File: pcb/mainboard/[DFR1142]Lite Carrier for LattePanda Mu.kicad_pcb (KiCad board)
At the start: 4 copper layers, 0 parts

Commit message: before i start jul 10th
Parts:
- added A1: LattePanda_Mu, Module_LattePanda:LattePanda_Module_H8.0mm_Horizontal, F.Cu at (148.0, 86.5)
- added BT1: Battery_Cell, A_HDJ_Library:Battery_Holder_CR1220_S8411-45R, F.Cu at (84.0, 114.3)
- added C17: 100nF/50V, A_HDJ_Library:C_0402_1005Metric, F.Cu at (172.5, 94.0)
- added C18: 100nF/50V, A_HDJ_Library:C_0402_1005Metric, F.Cu at (171.5, 94.0)
- added C19: 100nF/50V, A_HDJ_Library:C_0402_1005Metric, F.Cu at (170.5, 94.0)
- added C20: 100nF/50V, A_HDJ_Library:C_0402_1005Metric, F.Cu at (169.5, 94.0)
- added C21: 100nF/50V, A_HDJ_Library:C_0402_1005Metric, F.Cu at (168.5, 94.0)
- added C22: 100nF/50V, A_HDJ_Library:C_0402_1005Metric, F.Cu at (167.5, 94.0)
- added C23: 100nF/50V, A_HDJ_Library:C_0402_1005Metric, F.Cu at (166.5, 94.0)
- added C24: 100nF/50V, A_HDJ_Library:C_0402_1005Metric, F.Cu at (165.5, 94.0)
- added C25: 100nF/50V, A_HDJ_Library:C_0402_1005Metric, F.Cu at (17.4, 95.5)
- added C26: 100nF/50V, A_HDJ_Library:C_0402_1005Metric, F.Cu at (117.5, 93.5)
- added C27: 100nF/50V, A_HDJ_Library:C_0402_1005Metric, F.Cu at (116.5, 93.5)
- added C28: 100nF/50V, A_HDJ_Library:C_0402_1005Metric, F.Cu at (120.0, 93.5)
- added C29: 100nF/50V, A_HDJ_Library:C_0402_1005Metric, F.Cu at (119.0, 93.5)
- added C30: 22uF/10V, A_HDJ_Library:C_0603_1608Metric, F.Cu at (185.0, 113.0)
- added C31: 22uF/10V, A_HDJ_Library:C_0603_1608Metric, F.Cu at (179.0, 146.0)
- added C32: 22uF/10V, A_HDJ_Library:C_0603_1608Metric, F.Cu at (179.0, 130.0)
- added C49: 220nF/50V, A_HDJ_Library:C_0402_1005Metric, F.Cu at (141.0, 131.5)
- added C50: 220nF/50V, A_HDJ_Library:C_0402_1005Metric, F.Cu at (142.0, 131.5)
- added C51: 10uF/10V, A_HDJ_Library:C_0402_1005Metric, F.Cu at (132.5, 131.0)
- added C52: 100nF/50V, A_HDJ_Library:C_0402_1005Metric, F.Cu at (132.5, 132.0)
- added C53: 10uF/10V, A_HDJ_Library:C_0402_1005Metric, F.Cu at (132.5, 129.0)
- added C54: 100nF/50V, A_HDJ_Library:C_0402_1005Metric, F.Cu at (132.5, 130.0)
- added C55: 220nF/50V, A_HDJ_Library:C_0402_1005Metric, F.Cu at (120.4, 116.8)
- added C56: 220nF/50V, A_HDJ_Library:C_0402_1005Metric, F.Cu at (120.4, 117.8)
- added C57: 10uF/10V, A_HDJ_Library:C_0402_1005Metric, F.Cu at (113.4, 133.8)
- added C58: 100nF/50V, A_HDJ_Library:C_0402_1005Metric, F.Cu at (113.4, 132.8)
- added C59: 10uF/10V, A_HDJ_Library:C_0402_1005Metric, F.Cu at (113.4, 131.8)
- added C60: 100nF/50V, A_HDJ_Library:C_0402_1005Metric, F.Cu at (113.4, 130.8)
- added C64: 22uF/10V, A_HDJ_Library:C_0603_1608Metric, F.Cu at (22.5, 113.8)
- added C65: 22uF/10V, A_HDJ_Library:C_0603_1608Metric, F.Cu at (28.0, 138.5)
- added C66: 1uF/16V, A_HDJ_Library:C_0402_1005Metric, F.Cu at (14.5, 25.5)
- added C67: 22uF/10V, A_HDJ_Library:C_0603_1608Metric, F.Cu at (24.0, 113.8)
- added C68: 22uF/10V, A_HDJ_Library:C_0603_1608Metric, F.Cu at (28.0, 137.0)
- added C70: 100nF/50V, A_HDJ_Library:C_0402_1005Metric, F.Cu at (18.5, 110.0)
- added C71: 100nF/50V, A_HDJ_Library:C_0402_1005Metric, F.Cu at (23.5, 136.0)
- added C72: 12pF/50V, Capacitor_SMD:C_0402_1005Metric, F.Cu at (-38.2, 97.7)
- added C73: 12pF/50V, Capacitor_SMD:C_0402_1005Metric, F.Cu at (-38.2, 99.7)
- added C74: 22uF/10V, A_HDJ_Library:C_0603_1608Metric, F.Cu at (25.7, 107.0)
- added C75: 22uF/10V, A_HDJ_Library:C_0603_1608Metric, F.Cu at (31.8, 136.0)
- added C76: 22uF/10V, A_HDJ_Library:C_0603_1608Metric, F.Cu at (25.7, 108.5)
- added C77: 22uF/10V, A_HDJ_Library:C_0603_1608Metric, F.Cu at (31.8, 134.5)
- added C78: 100nF/50V, A_HDJ_Library:C_0402_1005Metric, F.Cu at (25.7, 102.5)
- added C79: 100nF/50V, A_HDJ_Library:C_0402_1005Metric, F.Cu at (31.8, 137.5)
- added C80: 22uF/10V, A_HDJ_Library:C_0603_1608Metric, F.Cu at (25.7, 104.0)
- added C81: 22uF/10V, A_HDJ_Library:C_0603_1608Metric, F.Cu at (31.8, 131.5)
- added C82: 22uF/10V, A_HDJ_Library:C_0603_1608Metric, F.Cu at (25.7, 105.5)
- added C83: 22uF/10V, A_HDJ_Library:C_0603_1608Metric, F.Cu at (31.8, 133.0)
- added C86: 22uF/10V, A_HDJ_Library:C_0603_1608Metric, F.Cu at (194.2, 80.5)
- added D1: ESD5V0B03, A_HDJ_Library:D_0402_1005Metric, F.Cu at (186.0, 98.5)
- added D15: SS54, A_HDJ_Library:D_SMA, F.Cu at (25.5, 120.5)
- added D16: SS54, A_HDJ_Library:D_SMA, F.Cu at (29.0, 120.5)
- added D17: SS54, A_HDJ_Library:D_SMA, F.Cu at (32.5, 120.5)
- added D2: ESD5V0B03, A_HDJ_Library:D_0402_1005Metric, F.Cu at (186.5, 102.5)
- added D21: ESD5V0B03, A_HDJ_Library:D_0402_1005Metric, F.Cu at (19.5, 25.5)
- added D22: LED_G, A_HDJ_Library:LED_0603_1608Metric, F.Cu at (-8.50, 85.5)
- added D24: 3V3 Izt=5mA, A_HDJ_Library:D_SOD-323, F.Cu at (-25.8, 103.9)
- added D3: ESD5V0B03, A_HDJ_Library:D_0402_1005Metric, F.Cu at (186.0, 99.5)
- added D4: 1N5819WS, A_HDJ_Library:D_SOD-323, F.Cu at (21.4, 75.0)
- added D5: ESD5V0B03, A_HDJ_Library:D_0402_1005Metric, F.Cu at (131.5, 93.5)
- added D6: ESD5V0B03, A_HDJ_Library:D_0402_1005Metric, F.Cu at (130.5, 93.5)
- added D7: ESD5V0B03, A_HDJ_Library:D_0402_1005Metric, F.Cu at (133.5, 93.5)
- added D8: ESD5V0B03, A_HDJ_Library:D_0402_1005Metric, F.Cu at (132.5, 93.5)
- added D9: LED_G, A_HDJ_Library:LED_0603_1608Metric, F.Cu at (131.0, 146.0)
- added F1: 6V/50mA, A_HDJ_Library:R_0603_1608Metric, F.Cu at (2.89, 95.9)
- added F2: 6V/1A, A_HDJ_Library:Fuse_0805_2012Metric, F.Cu at (188.5, 113.0)
- added F4: 6V/2A, A_HDJ_Library:R_0805_2012Metric, F.Cu at (183.1, 146.0)
- added F5: 6V/2A, A_HDJ_Library:Fuse_0805_2012Metric, F.Cu at (181.0, 127.0)
- added F78: 6V/1A, A_HDJ_Library:Fuse_0805_2012Metric, F.Cu at (197.0, 79.5)
- added FID1: Fiducial, A_HDJ_Library:Fiducial_0.5mm_Mask1mm, F.Cu at (50.0, 54.5)
- added FID2: Fiducial, A_HDJ_Library:Fiducial_0.5mm_Mask1mm, F.Cu at (50.0, 57.0)
- added H1: MountingHole_Pad, A_HDJ_Library:MountingHole_3.2mm_M3_Pad_Via, F.Cu at (171.0, 144.0)
- added H2: MountingHole_Pad, A_HDJ_Library:MountingHole_3.2mm_M3_Pad_Via, F.Cu at (194.5, 59.0)
- added H3: MountingHole_Pad, A_HDJ_Library:MountingHole_3.2mm_M3_Pad_Via, F.Cu at (109.5, 59.0)
- added H4: MountingHole_Pad, A_HDJ_Library:MountingHole_3.2mm_M3_Pad_Via, F.Cu at (110.0, 144.0)
- added H5: MountingHole_Pad, A_HDJ_Library:MountingHole_3mm_M2_Pad_TopOnly, F.Cu at (-20.1, 56.3)
- added H6: MountingHole_Pad, A_HDJ_Library:MountingHole_3mm_M2_Pad_TopOnly, F.Cu at (-20.1, 63.5)
- added J1: Conn_01x03_Pin, A_HDJ_Library:PinHeader_1x03_P2.54mm_Vertical, F.Cu at (118.0, 61.0)
- added J10: Conn_01x03_Pin, A_HDJ_Library:PinHeader_1x03_P2.54mm_Vertical, F.Cu at (143.5, 63.0)
- added J11: Conn_01x03_Pin, A_HDJ_Library:PinHeader_1x03_P2.54mm_Vertical, F.Cu at (139.8, 63.0)
- added J12: Conn_01x04_Pin, A_HDJ_Library:PinHeader_1x04_P2.54mm_Vertical, F.Cu at (154.2, 60.6)
- added J13: Conn_01x04_Pin, A_HDJ_Library:PinHeader_1x04_P2.54mm_Vertical, F.Cu at (154.2, 57.0)
- added J14: Conn_01x03_Pin, A_HDJ_Library:PinHeader_1x03_P2.54mm_Vertical, F.Cu at (136.1, 63.0)
- added J15: Bus_M.2_Socket_M, A_HDJ_Library:PCIe_M.2_Connectors_P=0.5mm_H=4.2mm_KeyM, F.Cu at (139.0, 139.0)
- added J16: Bus_M.2_Socket_E, A_HDJ_Library:PCIe_M.2_Connectors_P=0.5mm_H=4.2mm_KeyE, F.Cu at (116.9, 108.8)
- added J3: HDMI_A, A_HDJ_Library:HDMI_A_Molex_208658-1001_Horizontal, F.Cu at (192.6, 94.8)
- added J7: Conn_01x04_Pin, A_HDJ_Library:PinHeader_1x04_P2.54mm_Vertical, F.Cu at (167.7, 60.6)
- added J78: Conn_01x02_Pin, Connector_PinHeader_2.54mm:PinHeader_1x02_P2.54mm_Vertical, F.Cu at (-33.8, 101.6)
- added J79: USB3_A, Connector_USB:USB3_A_Molex_48393-001, F.Cu at (189.3, 143.0)
- added J8: Conn_01x03_Pin, A_HDJ_Library:PinHeader_1x03_P2.54mm_Vertical, F.Cu at (147.1, 63.0)
- added J80: USB3_A, Connector_USB:USB3_A_Molex_48393-001, F.Cu at (189.3, 127.0)
- added J81: USB_C_Receptacle_USB2.0_16P, Connector_USB:USB_C_Receptacle_GCT_USB4085, F.Cu at (192.6, 112.7)
- added J82: Conn_01x04_Pin, Connector_PinHeader_2.54mm:PinHeader_1x04_P2.54mm_Vertical, F.Cu at (193.5, 77.1)
- added J83: Conn_01x02_Pin, Connector_PinHeader_2.54mm:PinHeader_1x02_P2.54mm_Vertical, F.Cu at (17.0, 26.5)
- added J9: Conn_01x04_Pin, A_HDJ_Library:PinHeader_1x04_P2.54mm_Vertical, F.Cu at (167.7, 57.0)
- added JP1: Jumper_3_Bridged12, A_HDJ_Library:PinHeader_1x03_P2.54mm_Vertical, F.Cu at (13.0, 139.0)
- added L1: 2.2uH/4.3A, A_HDJ_Library:L_Sunlord_SWPA4020S, F.Cu at (21.0, 106.5)
- added L2: 2.2uH/4.3A, A_HDJ_Library:L_Sunlord_SWPA4020S, F.Cu at (26.5, 133.0)
- added Q1: 2N7002, A_HDJ_Library:SOT-23, F.Cu at (181.5, 102.0)
- added Q2: 2SK3018, A_HDJ_Library:SOT-23, F.Cu at (7.81, 83.3)
- added Q3: 2SK3018, A_HDJ_Library:SOT-23, F.Cu at (185.1, 106.0)
- added Q4: 2SK3018, A_HDJ_Library:SOT-23, F.Cu at (168.5, 105.4)
- added Q8: 2N7002, A_HDJ_Library:SOT-23, F.Cu at (-11.5, 84.5)
- added R1: 1K/1%, A_HDJ_Library:R_0402_1005Metric, F.Cu at (-15.0, 53.7)
- added R10: 470R/1%, A_HDJ_Library:R_0402_1005Metric, F.Cu at (168.5, 101.5)
- added R11: 1K/1%, A_HDJ_Library:R_0402_1005Metric, F.Cu at (186.0, 101.0)
- added R13: 470R/1%, A_HDJ_Library:R_0402_1005Metric, F.Cu at (169.5, 101.5)
- added R14: 470R/1%, A_HDJ_Library:R_0402_1005Metric, F.Cu at (170.5, 101.5)
- added R15: 2.2K/1%, A_HDJ_Library:R_0402_1005Metric, F.Cu at (18.5, 77.0)
- added R16: 470R/1%, A_HDJ_Library:R_0402_1005Metric, F.Cu at (171.5, 101.5)
- added R17: 470R/1%, A_HDJ_Library:R_0402_1005Metric, F.Cu at (172.5, 101.5)
- added R18: 2.2K/1%, A_HDJ_Library:R_0402_1005Metric, F.Cu at (17.5, 77.0)
- added R19: 2.2K/1%, A_HDJ_Library:R_0402_1005Metric, F.Cu at (167.0, 108.0)
- added R2: 10K/1%, A_HDJ_Library:R_0402_1005Metric, F.Cu at (147.5, 93.5)
- added R27: 0R/1%, A_HDJ_Library:R_0402_1005Metric, F.Cu at (143.5, 146.0)
- added R29: 0R/1%, A_HDJ_Library:R_0402_1005Metric, F.Cu at (147.5, 146.0)
- added R3: 2.2K/1%, A_HDJ_Library:R_0402_1005Metric, F.Cu at (11.7, 83.6)
- added R30: 2.2K/1%, A_HDJ_Library:R_0402_1005Metric, F.Cu at (134.5, 146.0)
- added R32: 0R/1%, A_HDJ_Library:R_0402_1005Metric, F.Cu at (120.0, 121.5)
- added R33: 0R/1%, A_HDJ_Library:R_0402_1005Metric, F.Cu at (106.5, 121.5)
- added R34: 10K/1%, A_HDJ_Library:R_0402_1005Metric, F.Cu at (109.4, 131.8)
- added R35: 10K/1%, A_HDJ_Library:R_0402_1005Metric, F.Cu at (109.4, 133.1)
- added R4: 1M/1%, A_HDJ_Library:R_0402_1005Metric, F.Cu at (179.0, 102.0)
- added R46: 100R/1%, A_HDJ_Library:R_0402_1005Metric, F.Cu at (29.0, 140.0)
- added R47: 1K/1%, A_HDJ_Library:R_0402_1005Metric, F.Cu at (-20.9, 98.7)
- added R48: 100R/1%, A_HDJ_Library:R_0402_1005Metric, F.Cu at (20.0, 23.5)
- added R49: 10K/1%, A_HDJ_Library:R_0402_1005Metric, F.Cu at (-14.5, 84.5)
- added R5: 2.2K/1%, A_HDJ_Library:R_0402_1005Metric, F.Cu at (11.7, 87.6)
- added R50: 10K/1%, Resistor_SMD:R_0402_1005Metric, F.Cu at (20.0, 22.0)
- added R51: 100K/1%, A_HDJ_Library:R_0402_1005Metric, F.Cu at (26.5, 140.5)
- added R52: 2.2K/1%, A_HDJ_Library:R_0402_1005Metric, F.Cu at (-8.00, 87.5)
- added R53: 2.2K/1%, A_HDJ_Library:R_0402_1005Metric, F.Cu at (-18.0, 100.7)
- added R57: 75K/1%, A_HDJ_Library:R_0402_1005Metric, F.Cu at (17.5, 115.5)
- added R58: 10K/1%, A_HDJ_Library:R_0402_1005Metric, F.Cu at (17.5, 116.5)
- added R59: 21.5K/1%, A_HDJ_Library:R_0402_1005Metric, F.Cu at (23.5, 141.5)
- added R6: 21.5K/1%, A_HDJ_Library:R_0402_1005Metric, F.Cu at (184.5, 102.0)
- added R60: 4.7K/1%, A_HDJ_Library:R_0402_1005Metric, F.Cu at (20.5, 139.0)
- added R7: 470R/1%, A_HDJ_Library:R_0402_1005Metric, F.Cu at (165.5, 101.5)
- added R76: 100K/1%, A_HDJ_Library:R_0402_1005Metric, F.Cu at (-15.0, 57.7)
- added R77: 100K/1%, A_HDJ_Library:R_0402_1005Metric, F.Cu at (-15.0, 59.7)
- added R78: 10K/1%, Resistor_SMD:R_0402_1005Metric, F.Cu at (-15.0, 61.7)
- added R79: 10K/1%, Resistor_SMD:R_0402_1005Metric, F.Cu at (-15.0, 63.7)
- added R8: 470R/1%, A_HDJ_Library:R_0402_1005Metric, F.Cu at (166.5, 101.5)
- added R80: 5.1K/1%, A_HDJ_Library:R_0402_1005Metric, F.Cu at (189.5, 110.5)
- added R81: 5.1K/1%, A_HDJ_Library:R_0402_1005Metric, F.Cu at (189.5, 109.5)
- added R9: 470R/1%, A_HDJ_Library:R_0402_1005Metric, F.Cu at (167.5, 101.5)
- added TP13: TestPoint, A_HDJ_Library:TestPoint_Pad_D1.5mm, F.Cu at (-37.9, 89.0)
- added TP2: TestPoint, A_HDJ_Library:TestPoint_Pad_D1.5mm, F.Cu at (123.0, 143.0)
- added TP4: TestPoint, A_HDJ_Library:TestPoint_Pad_D1.5mm, F.Cu at (-37.9, 78.4)
- added TP5: TestPoint, A_HDJ_Library:TestPoint_Pad_D1.5mm, F.Cu at (-37.9, 82.0)
- added TP6: TestPoint, A_HDJ_Library:TestPoint_Pad_D1.5mm, F.Cu at (-37.9, 85.5)
- added TP7: TestPoint, A_HDJ_Library:TestPoint_Pad_D1.5mm, F.Cu at (150.5, 94.5)
- added U1: TPAZ1023-04F, A_HDJ_Library:Diodes_UDFN-10_1.0x2.5mm_P0.5mm, F.Cu at (193.5, 84.9)
- added U10: ULC0524P, A_HDJ_Library:Diodes_UDFN-10_1.0x2.5mm_P0.5mm, F.Cu at (144.6, 55.2)
- added U11: ULC0524P, A_HDJ_Library:Diodes_UDFN-10_1.0x2.5mm_P0.5mm, F.Cu at (178.1, 56.5)
- added U12: ULC0524P, A_HDJ_Library:Diodes_UDFN-10_1.0x2.5mm_P0.5mm, F.Cu at (141.1, 55.2)
- added U15: SY8253ADC, A_HDJ_Library:TSOT-23-6, F.Cu at (18.4, 112.5)
- added U16: SY8253ADC, A_HDJ_Library:TSOT-23-6, F.Cu at (23.5, 138.5)
- added U2: TPAZ1023-04F, A_HDJ_Library:Diodes_UDFN-10_1.0x2.5mm_P0.5mm, F.Cu at (197.5, 84.9)
- added U3: ULC0524P, A_HDJ_Library:Diodes_UDFN-10_1.0x2.5mm_P0.5mm, F.Cu at (182.6, 133.0)
- added U4: ULC0524P, A_HDJ_Library:Diodes_UDFN-10_1.0x2.5mm_P0.5mm, F.Cu at (197.5, 73.3)
- added U5: ULC0524P, A_HDJ_Library:Diodes_UDFN-10_1.0x2.5mm_P0.5mm, F.Cu at (183.1, 122.0)
- added U9: ULC0524P, A_HDJ_Library:Diodes_UDFN-10_1.0x2.5mm_P0.5mm, F.Cu at (178.1, 61.5)
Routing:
- net /Gigabit Ethernet/MDI3+: track 2.23 -> 0.00 mm
- net /Gigabit Ethernet/MDI1-: track 1.67 -> 0.00 mm
- net /Gigabit Ethernet/MDI1+: track 1.58 -> 0.00 mm
- net /Gigabit Ethernet/MDI2-: track 1.30 -> 0.00 mm
- net /Gigabit Ethernet/MDI2+: track 1.21 -> 0.00 mm
- net /Gigabit Ethernet/MDI0+: track 0.97 -> 0.00 mm
- net /LattePanda Module/HSIO_9_TX+: track 0.97 -> 0.00 mm
- net /LattePanda Module/HSIO_11_TX+: track 0.97 -> 0.00 mm
- net /LattePanda Module/HSIO_10_TX+: track 0.97 -> 0.00 mm
- net /LattePanda Module/HSIO_9_TX-: track 0.97 -> 0.00 mm
- net /LattePanda Module/HSIO_11_TX-: track 0.97 -> 0.00 mm
- net /LattePanda Module/HSIO_10_TX-: track 0.97 -> 0.00 mm
- net /USB2.0&USB3.0/CON_USB4_D_N: track 0.89 -> 0.00 mm
- net /USB2.0&USB3.0/CON_USB3_D_N: track 0.89 -> 0.00 mm
- net /LattePanda Module/HSIO_1_TX+: track 0.89 -> 0.00 mm
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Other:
- board outline added: 95 x 95 mm
- copper layers 4 -> 2
- board text added: "0 1 2"
- board text added: "2 3 4 5"
- board text added: "3v3"
- board text added: "Dbg uart tx rx gnd"
- board text added: "E key"
- board text added: "GND"
- board text added: "I2C"
- board text added: "M key"
- board text added: "ON BTN"
- board text added: "RX"
- board text added: "SCL"
- board text added: "SDA"
- board text added: "TX"
- board text added: "UART"
- board text added: "board size: 95mmx95mm"

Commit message: ready for routing
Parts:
- removed FID1, FID2: Fiducial, A_HDJ_Library:Fiducial_0.5mm_Mask1mm
- moved F1 182.6 mm to (185.5, 99.5)
- moved R76 182.6 mm to (164.0, 93.5), turned to -90 degrees
- moved R77 181.2 mm to (163.0, 93.5), turned to -90 degrees
- moved C25 167.1 mm to (184.5, 97.5), turned to 90 degrees
- moved R1 163.0 mm to (143.0, 93.5), turned to -90 degrees
- moved R78 145.5 mm to (130.5, 61.5), turned to 90 degrees
- moved R79 144.5 mm to (129.5, 61.5), turned to 90 degrees
- moved C73 75.1 mm to (23.5, 142.5), turned to 180 degrees
- moved J78 64.8 mm to (31.0, 103.5), turned to 90 degrees
- moved C72 64.0 mm to (24.5, 110.5), turned to -90 degrees
- moved TP13 56.7 mm to (17.5, 101.5)
- moved D24 46.9 mm to (21.0, 101.5)
- moved R53 39.0 mm to (20.9, 103.0), turned to 180 degrees
- moved R47 18.9 mm to (-12.0, 82.0), turned to 180 degrees
- moved D17 11.5 mm to (32.5, 109.0), turned to 180 degrees
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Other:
- copper layers 2 -> 4

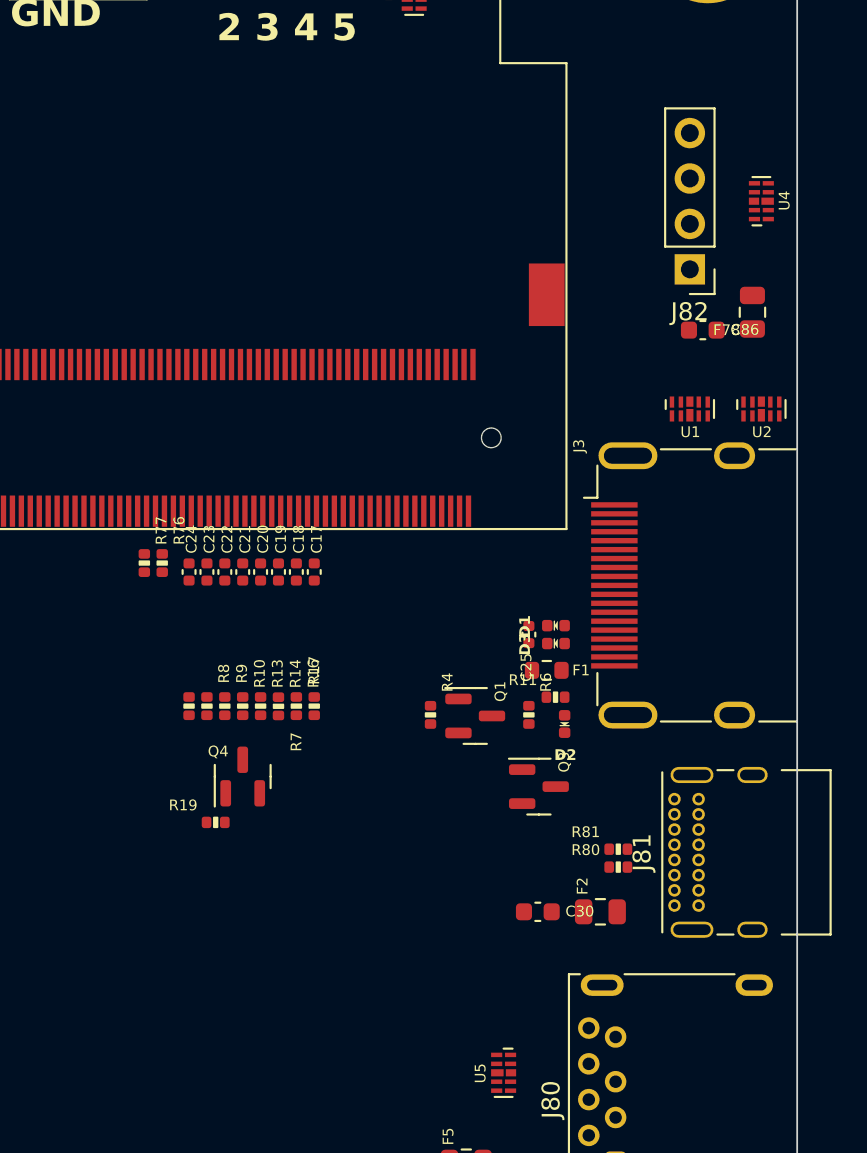
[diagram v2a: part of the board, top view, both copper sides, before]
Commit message: added extra esd to schem but not pcb also routed differential pairs of hdmi
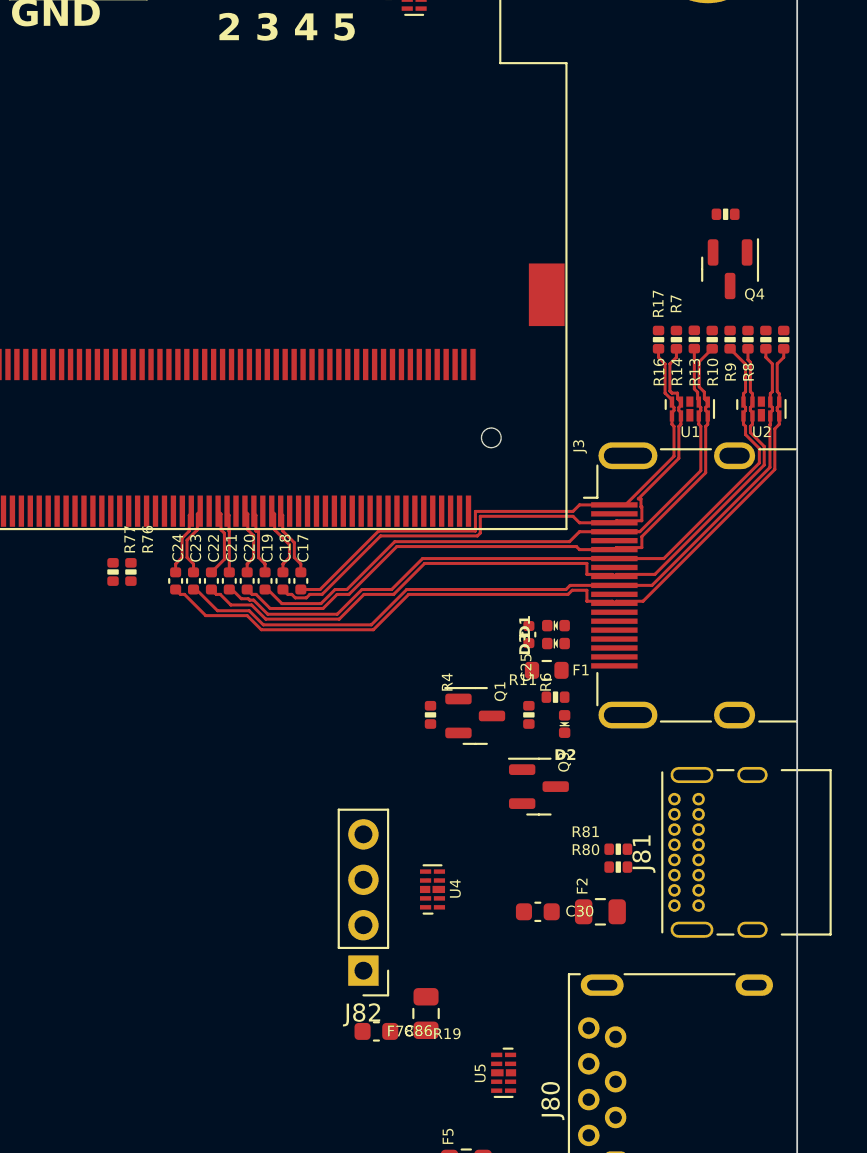
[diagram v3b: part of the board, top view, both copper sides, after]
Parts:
- moved R19 44.4 mm to (195.5, 74.0)
- moved J82 43.2 mm to (175.2, 116.3)
- moved C86 43.2 mm to (176.0, 119.7)
- moved F78 43.2 mm to (178.8, 118.7)
- moved U4 42.6 mm to (179.1, 111.8)
- moved Q4 39.3 mm to (195.8, 77.1), turned to -90 degrees
- moved R7 39.1 mm to (198.8, 81.0), turned to 90 degrees
- moved R8 37.4 mm to (197.8, 81.0), turned to 90 degrees
- moved R9 35.7 mm to (196.8, 81.0), turned to 90 degrees
- moved R10 34.1 mm to (195.8, 81.0), turned to 90 degrees
- moved R13 32.5 mm to (194.8, 81.0), turned to 90 degrees
- moved R14 31.0 mm to (193.8, 81.0), turned to 90 degrees
- moved R16 29.5 mm to (192.8, 81.0), turned to 90 degrees
- moved R17 28.1 mm to (191.8, 81.0)
- moved R76 1.82 mm to (162.2, 94.0)
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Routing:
- net /HDMI/TMDS_CK-: track 0.00 -> 46.3 mm
- net /HDMI/TMDS_CK+: track 0.00 -> 43.6 mm
- net /HDMI/TMDS_D0-: track 0.00 -> 43.2 mm
- net /HDMI/TMDS_D0+: track 0.00 -> 41.0 mm
- net /HDMI/TMDS_D1-: track 0.00 -> 37.3 mm
- net /HDMI/TMDS_D1+: track 0.00 -> 34.8 mm
- net /HDMI/TMDS_D2-: track 0.00 -> 34.4 mm
- net /HDMI/TMDS_D2+: track 0.00 -> 31.1 mm
- net /HDMI/DDI_B_TX0-: track 0.00 -> 3.98 mm
- net /HDMI/DDI_B_TX0+: track 0.00 -> 3.89 mm
- net /HDMI/DDI_B_TX3+: track 0.00 -> 3.88 mm
- net /HDMI/DDI_B_TX2-: track 0.00 -> 3.87 mm
- net /HDMI/DDI_B_TX3-: track 0.00 -> 3.78 mm
- net /HDMI/DDI_B_TX1-: track 0.00 -> 3.77 mm
- net /HDMI/DDI_B_TX1+: track 0.00 -> 3.76 mm
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
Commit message: gtg leave
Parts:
- added FID1: Fiducial, A_HDJ_Library:Fiducial_0.5mm_Mask1mm, F.Cu at (130.2, 166.2)
- added FID2: Fiducial, A_HDJ_Library:Fiducial_0.5mm_Mask1mm, F.Cu at (130.2, 168.8)
- added U78: ULC0524P, A_HDJ_Library:Diodes_UDFN-10_1.0x2.5mm_P0.5mm, F.Cu at (236.3, 91.6)
- moved C86 72.4 mm to (240.7, 87.3), turned to 90 degrees
- moved F78 69.9 mm to (239.7, 84.5), turned to 180 degrees
- moved J82 68.2 mm to (237.3, 88.0), turned to -90 degrees
- moved C50 12.0 mm to (131.0, 136.2), turned to 0 degrees
- moved C49 11.5 mm to (131.0, 137.2), turned to 0 degrees
- moved U4 8.07 mm to (186.9, 109.5)
- moved TP7 7.52 mm to (143.5, 97.2)
- moved C56 6.79 mm to (124.0, 112.0), turned to -90 degrees
- moved J15 6.45 mm to (144.8, 136.1)
- moved C53 6.45 mm to (138.3, 126.0)
- moved C54 6.45 mm to (138.3, 127.0)
- moved C51 6.45 mm to (138.3, 128.1)
- moved C52 6.45 mm to (138.3, 129.1)
- moved D9 6.45 mm to (136.8, 143.1)
- moved R27 6.45 mm to (149.2, 143.1)
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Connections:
- U3 pad 1: /USB2.0&USB3.0/CON_USB4_SSTX_N -> /USB2.0&USB3.0/CON_USB3_SSRX_P
- U3 pad 10: /USB2.0&USB3.0/CON_USB4_SSTX_N -> /USB2.0&USB3.0/CON_USB3_SSRX_P
- U3 pad 2: /USB2.0&USB3.0/CON_USB4_SSTX_P -> /USB2.0&USB3.0/CON_USB3_SSRX_N
- U3 pad 4: /USB2.0&USB3.0/CON_USB3_SSTX_N -> /USB2.0&USB3.0/CON_USB3_SSTX_P
- U3 pad 5: /USB2.0&USB3.0/CON_USB3_SSTX_P -> /USB2.0&USB3.0/CON_USB3_SSTX_N
- U3 pad 6: /USB2.0&USB3.0/CON_USB3_SSTX_P -> /USB2.0&USB3.0/CON_USB3_SSTX_N
- U3 pad 7: /USB2.0&USB3.0/CON_USB3_SSTX_N -> /USB2.0&USB3.0/CON_USB3_SSTX_P
- U3 pad 9: /USB2.0&USB3.0/CON_USB4_SSTX_P -> /USB2.0&USB3.0/CON_USB3_SSRX_N
- U4 pad 4: /USB2.0&USB3.0/CON_USB2_D_P -> unconnected-(U4-NC-Pad7)
- U4 pad 5: /USB2.0&USB3.0/CON_USB2_D_N -> unconnected-(U4-NC-Pad6)
- U4 pad 6: /USB2.0&USB3.0/CON_USB2_D_N -> unconnected-(U4-NC-Pad6)
- U4 pad 7: /USB2.0&USB3.0/CON_USB2_D_P -> unconnected-(U4-NC-Pad7)
- U5 pad 4: /USB2.0&USB3.0/CON_USB3_SSRX_N -> /USB2.0&USB3.0/CON_USB4_SSTX_N
- U5 pad 5: /USB2.0&USB3.0/CON_USB3_SSRX_P -> /USB2.0&USB3.0/CON_USB4_SSTX_P
- U5 pad 6: /USB2.0&USB3.0/CON_USB3_SSRX_P -> /USB2.0&USB3.0/CON_USB4_SSTX_P
- U5 pad 7: /USB2.0&USB3.0/CON_USB3_SSRX_N -> /USB2.0&USB3.0/CON_USB4_SSTX_N
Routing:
- net /USB2.0&USB3.0/CON_USB3_SSRX_N: track 0.00 -> 156.7 mm
- net /USB2.0&USB3.0/CON_USB3_SSRX_P: track 0.00 -> 155.3 mm
- net /USB2.0&USB3.0/CON_USB3_SSTX_P: track 0.00 -> 128.6 mm
- net /USB2.0&USB3.0/CON_USB3_SSTX_N: track 0.00 -> 127.2 mm
- net /USB2.0&USB3.0/CON_USB4_SSTX_N: track 0.00 -> 120.3 mm
- net /USB2.0&USB3.0/CON_USB4_SSTX_P: track 0.00 -> 119.7 mm
- net /USB2.0&USB3.0/CON_USB4_SSRX_P: track 0.00 -> 92.1 mm
- net /USB2.0&USB3.0/CON_USB4_SSRX_N: track 0.00 -> 91.4 mm
- net /LattePanda Module/HSIO_3_TX-: track 0.00 -> 21.6 mm
- net /LattePanda Module/HSIO_3_TX+: track 0.00 -> 21.3 mm
- net /M.2 E&M Key/CON_PCIE_TX_1+: track 0.00 -> 18.8 mm
- net /M.2 E&M Key/CON_PCIE_TX_1-: track 0.00 -> 18.4 mm
- net /LattePanda Module/HSIO_2_TX+: track 0.00 -> 7.20 mm
- net /USB2.0&USB3.0/CON_USB1_D_N: track 0.00 -> 6.66 mm
- net /USB2.0&USB3.0/CON_USB1_D_P: track 0.00 -> 6.43 mm
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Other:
- board text added: "DONT FORGET TO CONNECT OTHER SIDE"

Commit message: restarted board hdmi done
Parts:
- moved J82 245.5 mm to (-0.37, 26.3), turned to 0 degrees
- moved Q4 231.4 mm to (-35.7, 78.8), turned to 0 degrees
- moved U78 230.7 mm to (15.2, 26.0), turned to 0 degrees
- moved R29 227.7 mm to (-1.21, -24.2)
- moved F1 226.7 mm to (-40.6, 82.5)
- moved F78 226.5 mm to (18.8, 34.3), turned to 0 degrees
- moved R27 226.4 mm to (-1.21, -26.2)
- moved R76 226.3 mm to (-58.5, 44.2), turned to 0 degrees
- moved R77 224.9 mm to (-58.5, 46.2), turned to 0 degrees
- moved C86 224.4 mm to (23.1, 32.8), turned to 0 degrees
- moved Q3 223.0 mm to (-35.7, 74.3)
- moved R19 221.5 mm to (-26.0, 72.1)
- moved D2 221.3 mm to (-31.8, 66.2), turned to 0 degrees
- moved D1 220.3 mm to (-31.8, 64.2)
- moved Q1 220.2 mm to (-35.7, 65.4)
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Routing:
- net /USB2.0&USB3.0/CON_USB3_SSRX_N: track 156.7 -> 0.00 mm
- net /USB2.0&USB3.0/CON_USB3_SSRX_P: track 155.3 -> 0.00 mm
- net /USB2.0&USB3.0/CON_USB3_SSTX_P: track 128.6 -> 0.00 mm
- net /USB2.0&USB3.0/CON_USB3_SSTX_N: track 127.2 -> 0.00 mm
- net /USB2.0&USB3.0/CON_USB4_SSTX_N: track 120.3 -> 0.00 mm
- net /USB2.0&USB3.0/CON_USB4_SSTX_P: track 119.7 -> 0.00 mm
- net /USB2.0&USB3.0/CON_USB4_SSRX_P: track 92.1 -> 0.00 mm
- net /USB2.0&USB3.0/CON_USB4_SSRX_N: track 91.4 -> 0.00 mm
- net /HDMI/TMDS_CK-: track 46.3 -> 22.0 mm
- net /HDMI/TMDS_D0-: track 43.2 -> 20.8 mm
- net /LattePanda Module/HSIO_3_TX-: track 21.6 -> 0.00 mm
- net /HDMI/TMDS_CK+: track 43.6 -> 22.2 mm
- net /LattePanda Module/HSIO_3_TX+: track 21.3 -> 0.00 mm
- net /HDMI/TMDS_D0+: track 41.0 -> 21.5 mm
- net /M.2 E&M Key/CON_PCIE_TX_1+: track 18.8 -> 0.00 mm
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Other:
- board size 95 x 95 mm -> 150 x 109 mm
- board text removed: "0 1 2"
- board text removed: "2 3 4 5"
- board text removed: "3v3"
- board text removed: "DONT FORGET TO CONNECT OTHER SIDE"
- board text removed: "Dbg uart tx rx gnd"
- board text removed: "E key"
- board text removed: "GND"
- board text removed: "I2C"
- board text removed: "M key"
- board text removed: "ON BTN"
- board text removed: "RX"
- board text removed: "SCL"
- board text removed: "SDA"
- board text removed: "TX"
- board text removed: "UART"
- board text removed: "board size: 95mmx95mm"

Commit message: a
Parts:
- moved C49 191.1 mm to (132.0, 138.5), turned to -90 degrees
- moved C50 190.3 mm to (133.0, 138.5), turned to -90 degrees
- moved C57 186.4 mm to (117.0, 149.5), turned to 90 degrees
- moved C58 185.4 mm to (118.0, 149.5), turned to 90 degrees
- moved C59 184.4 mm to (119.0, 149.5), turned to 90 degrees
- moved C60 183.4 mm to (120.0, 149.5), turned to 90 degrees
- moved C53 166.9 mm to (88.5, 143.0), turned to 180 degrees
- moved C54 164.3 mm to (88.5, 142.0), turned to 180 degrees
- moved C51 163.3 mm to (88.5, 141.0), turned to 180 degrees
- moved C52 160.8 mm to (88.5, 140.0), turned to 180 degrees
- moved J16 159.2 mm to (95.0, 118.0), turned to -90 degrees
- moved J15 41.7 mm to (109.0, 129.0)
- moved J80 37.1 mm to (99.5, 155.3)
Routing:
- net /M.2 E&M Key/CON_PCIE_TX_1-: track 0.00 -> 44.1 mm
- net /LattePanda Module/HSIO_3_RX-: track 0.00 -> 43.1 mm
- net /LattePanda Module/HSIO_3_RX+: track 0.00 -> 42.5 mm
- net /M.2 E&M Key/CON_PCIE_TX_1+: track 0.00 -> 42.3 mm
- net /LattePanda Module/HSIO_2_RX+: track 0.00 -> 30.0 mm, vias 0 -> 2
- net /LattePanda Module/HSIO_2_RX-: track 0.00 -> 29.7 mm, vias 0 -> 2
- net /LattePanda Module/HSIO_2_TX-: track 0.00 -> 3.79 mm
- net /LattePanda Module/HSIO_2_TX+: track 0.00 -> 3.70 mm
- net /LattePanda Module/REFCLK0-: track 0.00 -> 1.47 mm
- net /LattePanda Module/REFCLK0+: track 0.00 -> 1.47 mm
